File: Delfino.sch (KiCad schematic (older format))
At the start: 1 part

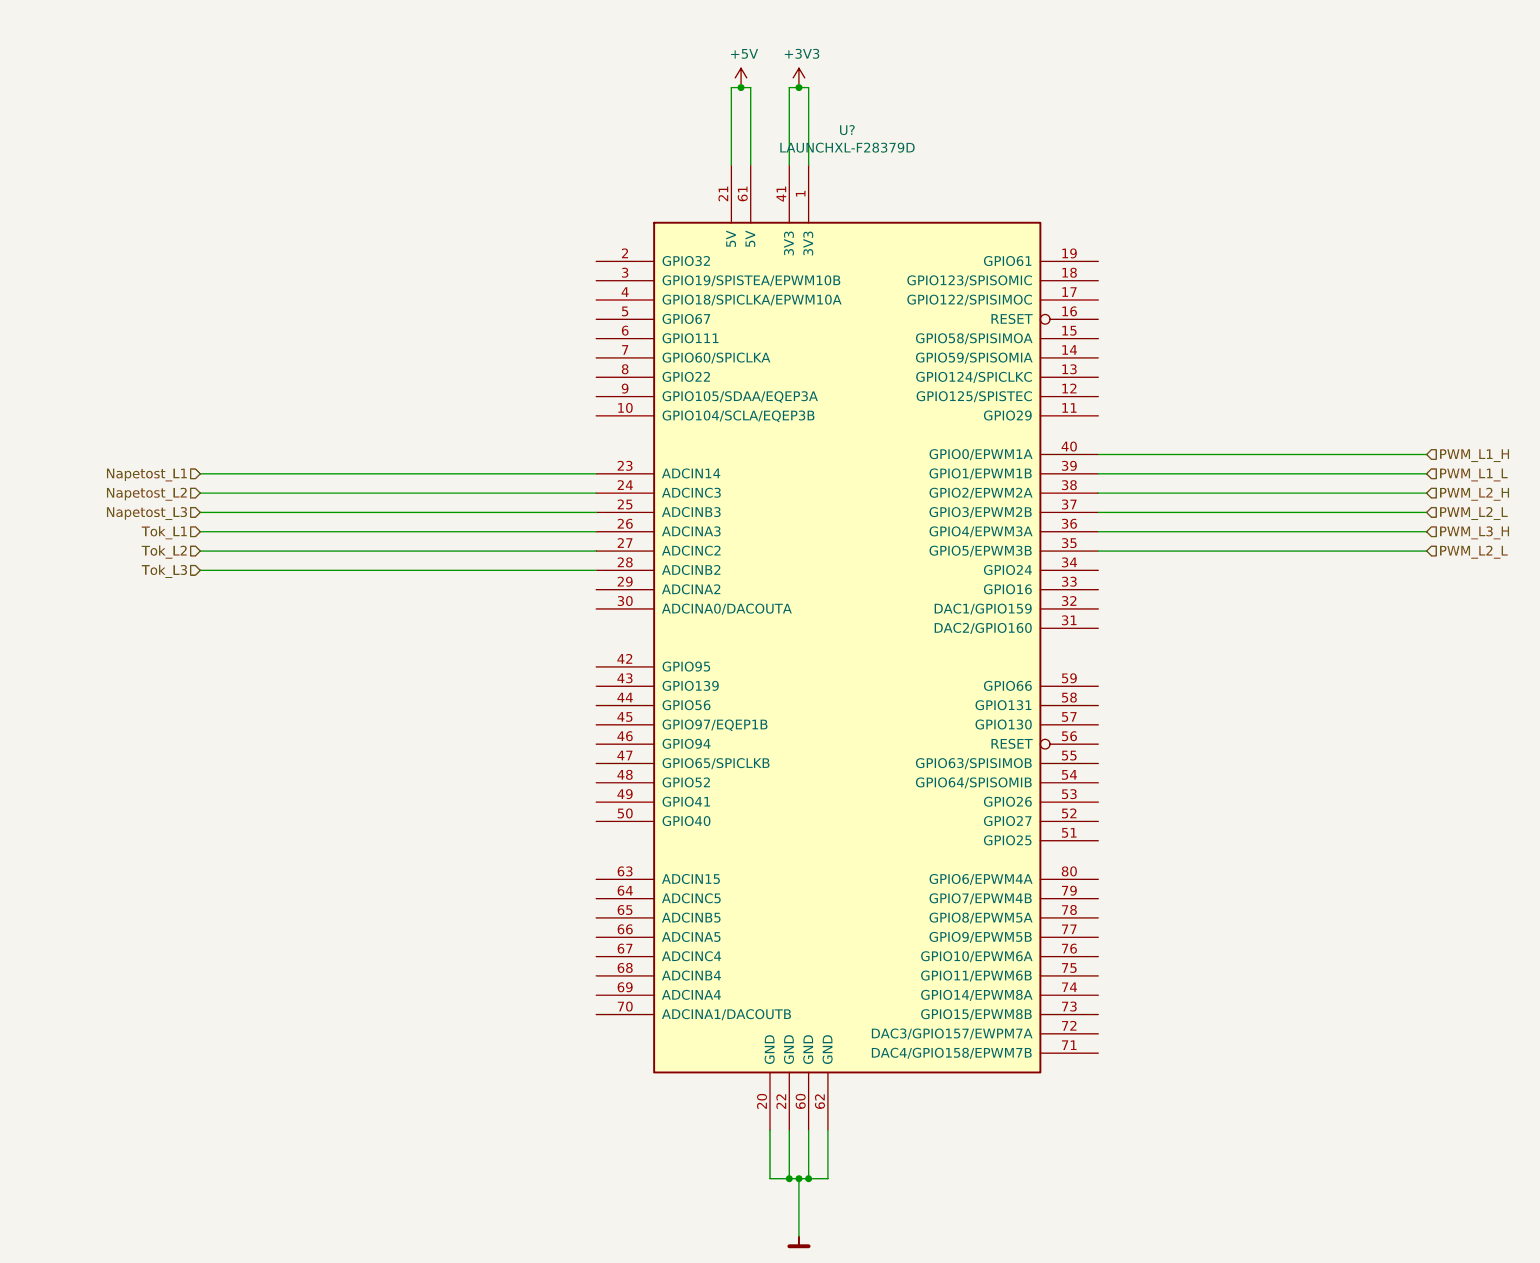
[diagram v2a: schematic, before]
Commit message: Narejene povezave med sheet-i, še vedno nevem kaj z QEP signali
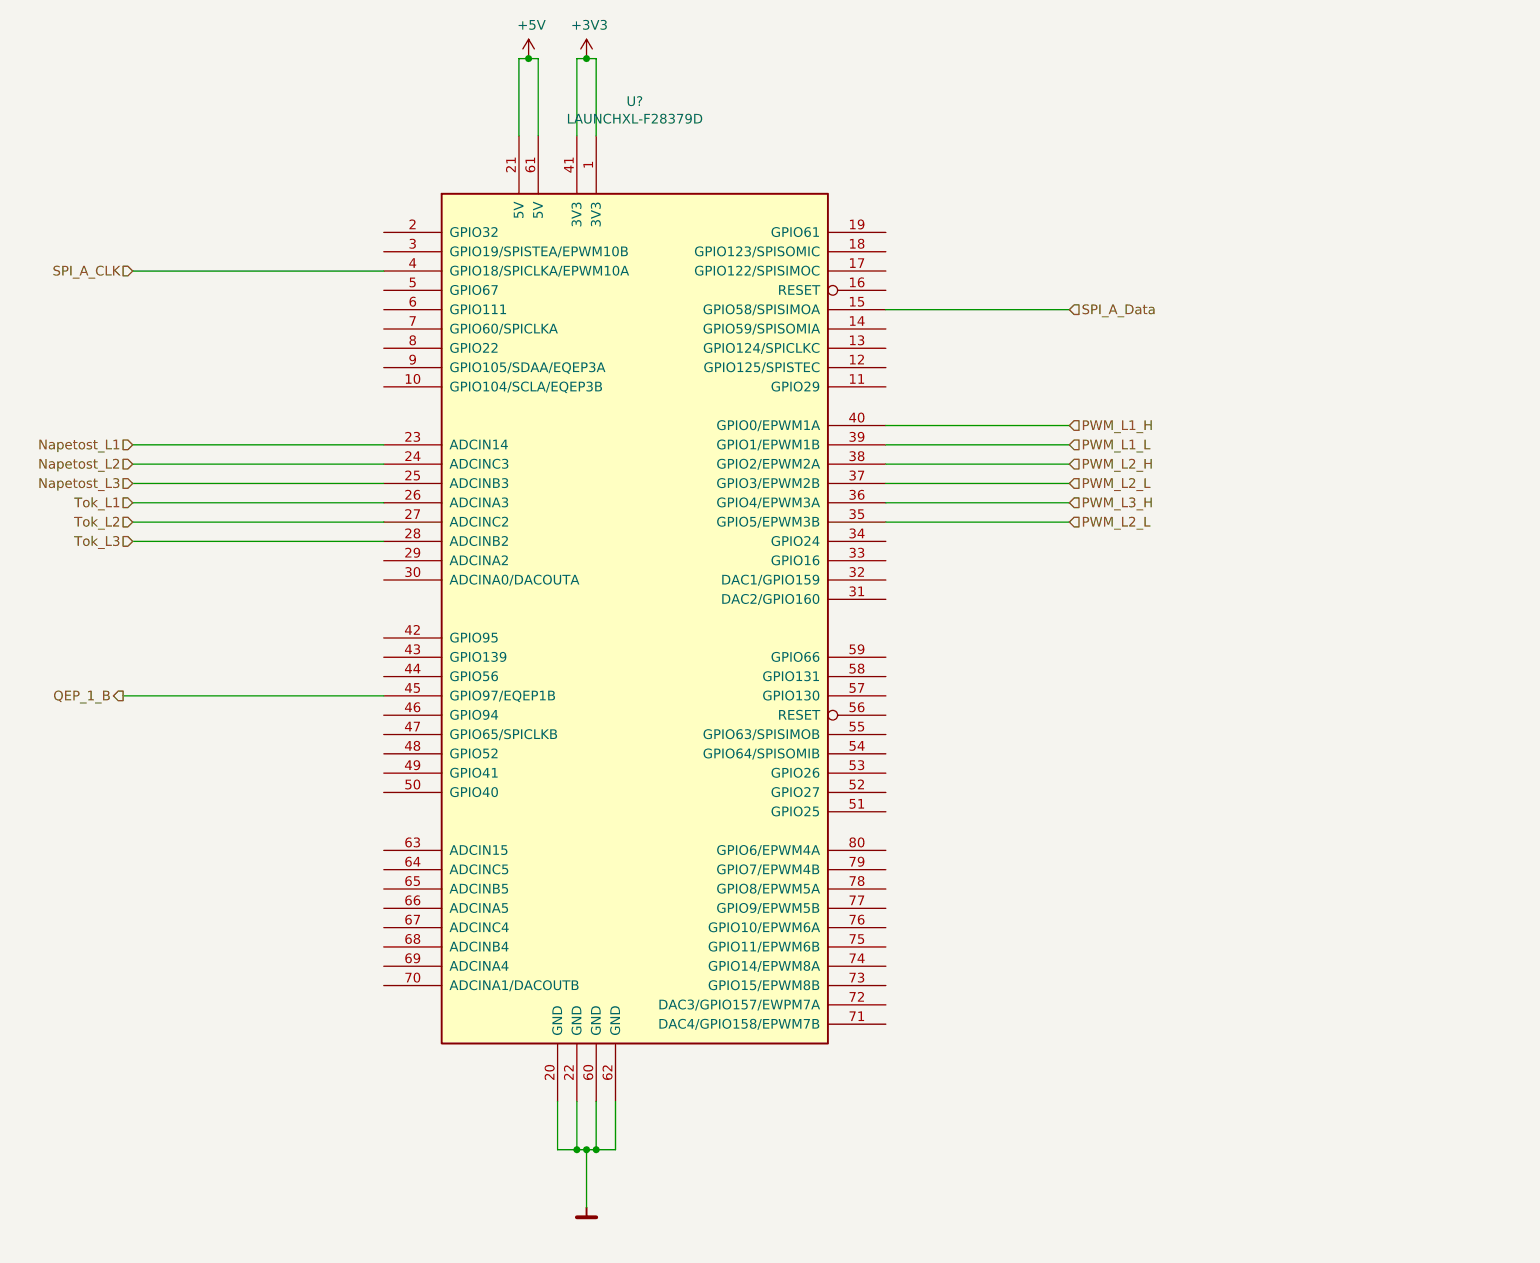
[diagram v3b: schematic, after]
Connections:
- net SPI_A_Data: now reaches U?.15 (GPIO58/SPISIMOA)
- net SPI_A_CLK: now reaches U?.4 (GPIO18/SPICLKA/EPWM10A)
- net QEP_1_B: now reaches U?.45 (GPIO97/EQEP1B)
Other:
- moved on the sheet: U?
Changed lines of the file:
@@
 $Descr A4 11693 8268
 encoding utf-8
-Sheet 2 5
+Sheet 2 7
 Title ""
 Date ""
@@
 L Module:LAUNCHXL-F28379D U?
 U 1 1 5BC6DEB5
-P 5550 3750
-F 0 "U?" H 5550 6428 50  0000 C CNN
-F 1 "LAUNCHXL-F28379D" H 5550 6337 50  0000 C CNN
-F 2 "Module:28379D_launchpad" H 5650 6050 50  0001 L CNN
-F 3 "http://www.ti.com/lit/ug/sprui77a/sprui77a.pdf" H 4550 6450 50  0001 L CNN
-	1    5550 3750
+P 4450 3600
+F 0 "U?" H 4450 6278 50  0000 C CNN
+F 1 "LAUNCHXL-F28379D" H 4450 6187 50  0000 C CNN
+F 2 "Module:28379D_launchpad" H 4550 5900 50  0001 L CNN
+F 3 "http://www.ti.com/lit/ug/sprui77a/sprui77a.pdf" H 3450 6300 50  0001 L CNN
+	1    4450 3600
 	1    0    0    -1
 $EndComp
 Wire Wire Line
-	5150 6250 5150 6500
+	4050 6100 4050 6350
 Wire Wire Line
-	5150 6500 5250 6500
+	4050 6350 4150 6350
 Wire Wire Line
-	5450 6500 5450 6250
+	4350 6350 4350 6100
 Wire Wire Line
-	5250 6250 5250 6500
-Connection ~ 5250 6500
+	4150 6100 4150 6350
+Connection ~ 4150 6350
 Wire Wire Line
-	5250 6500 5300 6500
+	4150 6350 4200 6350
 Wire Wire Line
-	5350 6250 5350 6500
-Connection ~ 5350 6500
+	4250 6100 4250 6350
+Connection ~ 4250 6350
 Wire Wire Line
-	5350 6500 5450 6500
+	4250 6350 4350 6350
 Wire Wire Line
-	5300 6500 5300 6800
-Connection ~ 5300 6500
+	4200 6350 4200 6650
+Connection ~ 4200 6350
 Wire Wire Line
-	5300 6500 5350 6500
+	4200 6350 4250 6350
 $Comp
 L Passives:GND #PWR?
 U 1 1 5BC6E15F
-P 5300 6800
-F 0 "#PWR?" H 5300 6650 50  0001 C CNN
-F 1 "GND" H 5450 6750 50  0001 C CNN
-F 2 "" H 5300 6800 50  0001 C CNN
-F 3 "" H 5300 6800 50  0001 C CNN
-	1    5300 6800
+P 4200 6650
+F 0 "#PWR?" H 4200 6500 50  0001 C CNN
+F 1 "GND" H 4350 6600 50  0001 C CNN
+F 2 "" H 4200 6650 50  0001 C CNN
+F 3 "" H 4200 6650 50  0001 C CNN
+	1    4200 6650
 	1    0    0    -1
 $EndComp
-Text HLabel 8550 2750 2    50   Input ~ 0
+Text HLabel 6700 2600 2    50   Input ~ 0
 PWM_L1_H
-Text HLabel 8550 2850 2    50   Input ~ 0
+Text HLabel 6700 2700 2    50   Input ~ 0
 PWM_L1_L
-Text HLabel 8550 2950 2    50   Input ~ 0
+Text HLabel 6700 2800 2    50   Input ~ 0
 PWM_L2_H
-Text HLabel 8550 3050 2    50   Input ~ 0
+Text HLabel 6700 2900 2    50   Input ~ 0
 PWM_L2_L
-Text HLabel 8550 3150 2    50   Input ~ 0
+Text HLabel 6700 3000 2    50   Input ~ 0
 PWM_L3_H
-Text HLabel 8550 3250 2    50   Input ~ 0
+Text HLabel 6700 3100 2    50   Input ~ 0
 PWM_L2_L
-Wire Wire Line
-	6850 2750 8550 2750
-Wire Wire Line
-	6850 2850 8550 2850
-Wire Wire Line
-	8550 2950 6850 2950
-Wire Wire Line
-	6850 3050 8550 3050
-Wire Wire Line
-	8550 3150 6850 3150
-Wire Wire Line
-	6850 3250 8550 3250
-Text HLabel 2200 2850 0    50   Input ~ 0
+Text HLabel 1850 2700 0    50   Input ~ 0
 Napetost_L1
-Text HLabel 2200 2950 0    50   Input ~ 0
+Text HLabel 1850 2800 0    50   Input ~ 0
 Napetost_L2
-Text HLabel 2200 3050 0    50   Input ~ 0
+Text HLabel 1850 2900 0    50   Input ~ 0
 Napetost_L3
-Wire Wire Line
-	4250 2850 2200 2850
-Wire Wire Line
-	2200 2950 4250 2950
-Wire Wire Line
-	4250 3050 2200 3050
 $Comp
 L power:+5V #PWR?
 U 1 1 5BC8755A
-P 5000 850
-F 0 "#PWR?" H 5000 700 50  0001 C CNN
-F 1 "+5V" H 5015 1023 50  0000 C CNN
-F 2 "" H 5000 850 50  0001 C CNN
-F 3 "" H 5000 850 50  0001 C CNN
-	1    5000 850
+P 3900 700
+F 0 "#PWR?" H 3900 550 50  0001 C CNN
+F 1 "+5V" H 3915 873 50  0000 C CNN
+F 2 "" H 3900 700 50  0001 C CNN
+F 3 "" H 3900 700 50  0001 C CNN
+	1    3900 700
 	1    0    0    -1
 $EndComp
 Wire Wire Line
-	4950 1250 4950 850
+	3850 1100 3850 700
 Wire Wire Line
-	4950 850  5000 850
+	3850 700  3900 700
 Wire Wire Line
-	5050 850  5050 1250
-Connection ~ 5000 850
+	3950 700  3950 1100
+Connection ~ 3900 700
 Wire Wire Line
-	5000 850  5050 850
+	3900 700  3950 700
 Wire Wire Line
-	5250 1250 5250 850
+	4150 1100 4150 700
 Wire Wire Line
-	5250 850  5300 850
+	4150 700  4200 700
 Wire Wire Line
-	5350 850  5350 1250
+	4250 700  4250 1100
 $Comp
 L power:+3V3 #PWR?
 U 1 1 5BC87A4C
-P 5300 850
-F 0 "#PWR?" H 5300 700 50  0001 C CNN
-F 1 "+3V3" H 5315 1023 50  0000 C CNN
-F 2 "" H 5300 850 50  0001 C CNN
-F 3 "" H 5300 850 50  0001 C CNN
-	1    5300 850
+P 4200 700
+F 0 "#PWR?" H 4200 550 50  0001 C CNN
+F 1 "+3V3" H 4215 873 50  0000 C CNN
+F 2 "" H 4200 700 50  0001 C CNN
+F 3 "" H 4200 700 50  0001 C CNN
+	1    4200 700
 	1    0    0    -1
 $EndComp
-Connection ~ 5300 850
+Connection ~ 4200 700
 Wire Wire Line
-	5300 850  5350 850
-Text HLabel 2200 3150 0    50   Input ~ 0
+	4200 700  4250 700
+Text HLabel 1850 3000 0    50   Input ~ 0
 Tok_L1
-Text HLabel 2200 3250 0    50   Input ~ 0
+Text HLabel 1850 3100 0    50   Input ~ 0
 Tok_L2
-Text HLabel 2200 3350 0    50   Input ~ 0
+Text HLabel 1850 3200 0    50   Input ~ 0
 Tok_L3
+Text HLabel 1850 1800 0    50   Input ~ 0
+SPI_A_CLK
+Text HLabel 6700 2000 2    50   Input ~ 0
+SPI_A_Data
+Text HLabel 1800 4000 0    50   Output ~ 0
+QEP_1_B
 Wire Wire Line
-	4250 3150 2200 3150
+	1850 1800 3150 1800
 Wire Wire Line
-	2200 3250 4250 3250
+	1850 2700 3150 2700
 Wire Wire Line
-	4250 3350 2200 3350
+	1850 2800 3150 2800
+Wire Wire Line
+	3150 2900 1850 2900
+Wire Wire Line
+	1850 3000 3150 3000
+Wire Wire Line
+	3150 3100 1850 3100
+Wire Wire Line
+	1850 3200 3150 3200
+Wire Wire Line
+	3150 4000 1800 4000
+Wire Wire Line
+	6700 3100 5750 3100
+Wire Wire Line
+	5750 3000 6700 3000
+Wire Wire Line
+	6700 2900 5750 2900
+Wire Wire Line
+	5750 2800 6700 2800
+Wire Wire Line
+	6700 2700 5750 2700
+Wire Wire Line
+	5750 2600 6700 2600
+Wire Wire Line
+	6700 2000 5750 2000
 $EndSCHEMATC
